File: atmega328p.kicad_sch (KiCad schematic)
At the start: 6 parts, among them J6 ICSP, U6 ATMEGA328PB-AU, Y1 CSTNE16M0VH3L000R0

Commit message: Replace CSTNE16M0VH3L000R0 ceramic resonator with HC49S quartz crystal and capacitors.
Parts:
- removed Y1: CSTNE16M0VH3L000R0, Crystal:Resonator_SMD_muRata_CSTxExxV-3Pin_3.0x1.1mm, symbol bkm-129x-scart-vga-rescue:Crystal_GND2
- added C14: 22pF, Capacitor_SMD:C_1206_3216Metric_Pad1.33x1.80mm_HandSolder, symbol bkm-129x-scart-vga-rescue:C
- added C18: 22pF, Capacitor_SMD:C_1206_3216Metric_Pad1.33x1.80mm_HandSolder, symbol Device:C
- added Y1: 16MHz, Crystal:Crystal_HC49-U_Vertical, symbol Device:Crystal
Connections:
- net GNDD: now also C14.2, C18.2
- net at U6.7 ((XTAL1/TOSC1)PB6): now also C14.1, Y1.2
- net at U6.8 ((XTAL2/TOSC2)PB7): now also C18.1, Y1.1

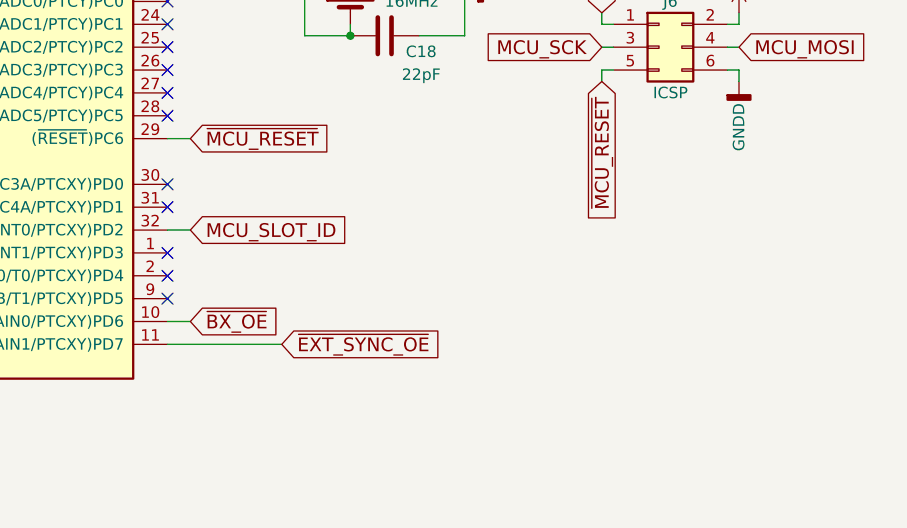
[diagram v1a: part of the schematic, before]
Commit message: Add debug UART connector to schematic and PCB. Edit silkscreen MCU description.
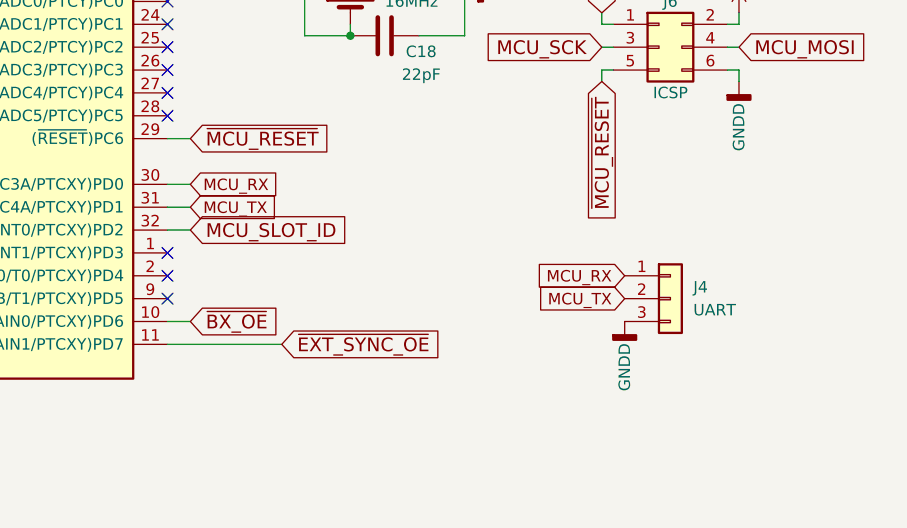
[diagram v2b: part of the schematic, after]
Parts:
- added J4: UART, Connector_PinHeader_2.54mm:PinHeader_1x03_P2.54mm_Vertical, symbol Connector_Generic:Conn_01x03
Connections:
- net GNDD: now also J4.3 (Pin_3)
- net MCU_RX: now reaches U6.30 ((RXD0/OC3A/PTCXY)PD0)
- net MCU_RX: now also J4.1 (Pin_1)
- net MCU_TX: now reaches U6.31 ((TXD0/OC4A/PTCXY)PD1)
- net MCU_TX: now also J4.2 (Pin_2)
- no-connect marks 17 -> 15
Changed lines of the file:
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@@
-	)
-	(no_connect
-		(at 163.83 101.6)
 	)
 	(no_connect
@@
 	)
 	(no_connect
-		(at 163.83 104.14)
-	)
-	(no_connect
 		(at 163.83 60.96)
 	)
@@
 	(wire
 		(pts
+			(xy 166.37 104.14) (xy 163.83 104.14)
+		)
+		(stroke
+			(width 0)
+			(type default)
+		)
+	)
+	(wire
+		(pts
 			(xy 163.83 96.52) (xy 166.37 96.52)
 		)
@@
 		(pts
 			(xy 184.15 74.93) (xy 184.15 76.2)
+		)
+		(stroke
+			(width 0)
+			(type default)
+		)
+	)
+	(wire
+		(pts
+			(xy 166.37 101.6) (xy 163.83 101.6)
 		)
 		(stroke
@@
 		)
 	)
+	(global_label "MCU_TX"
+		(shape input)
+		(at 214.63 114.3 180)
+		(fields_autoplaced yes)
+		(effects
+			(font
+				(size 1.27 1.27)
+			)
+			(justify right)
+		)
+		(property "Intersheetrefs" "${INTERSHEET_REFS}"
+			(at 205.1024 114.3 0)
+			(effects
+				(font
+					(size 1.27 1.27)
+				)
+				(justify right)
+				(hide yes)
+			)
+		)
+	)
 	(global_label "MCU_SCK"
 		(shape input)
@@
 		)
 	)
+	(global_label "MCU_RX"
+		(shape input)
+		(at 214.63 111.76 180)
+		(fields_autoplaced yes)
+		(effects
+			(font
+				(size 1.27 1.27)
+			)
+			(justify right)
+		)
+		(property "Intersheetrefs" "${INTERSHEET_REFS}"
+			(at 204.8 111.76 0)
+			(effects
+				(font
+					(size 1.27 1.27)
+				)
+				(justify right)
+				(hide yes)
+			)
+		)
+	)
 	(global_label "MCU_SLOT_ID"
 		(shape input)
@@
 		)
 	)
+	(global_label "MCU_RX"
+		(shape input)
+		(at 166.37 101.6 0)
+		(fields_autoplaced yes)
+		(effects
+			(font
+				(size 1.27 1.27)
+			)
+			(justify left)
+		)
+		(property "Intersheetrefs" "${INTERSHEET_REFS}"
+			(at 176.2 101.6 0)
+			(effects
+				(font
+					(size 1.27 1.27)
+				)
+				(justify left)
+				(hide yes)
+			)
+		)
+	)
 	(global_label "MCU_MISO"
 		(shape input)
@@
 					(size 1.27 1.27)
 				)
+				(hide yes)
+			)
+		)
+	)
+	(global_label "MCU_TX"
+		(shape input)
+		(at 166.37 104.14 0)
+		(fields_autoplaced yes)
+		(effects
+			(font
+				(size 1.27 1.27)
+			)
+			(justify left)
+		)
+		(property "Intersheetrefs" "${INTERSHEET_REFS}"
+			(at 175.8976 104.14 0)
+			(effects
+				(font
+					(size 1.27 1.27)
+				)
+				(justify left)
 				(hide yes)
 			)
@@
 				(path "/dd381a99-a14a-480e-874b-b22abf62e9bf/00000000-0000-0000-0000-00005fb20956"
 					(reference "C18")
+					(unit 1)
+				)
+			)
+		)
+	)
+	(symbol
+		(lib_id "bkm-129x-scart-vga-rescue:GNDD-power")
+		(at 214.63 116.84 0)
+		(unit 1)
+		(exclude_from_sim no)
+		(in_bom yes)
+		(on_board yes)
+		(dnp no)
+		(property "Reference" "#PWR06"
+			(at 214.63 123.19 0)
+			(effects
+				(font
+					(size 1.27 1.27)
+				)
+				(hide yes)
+			)
+		)
+		(property "Value" "GNDD"
+			(at 214.63 121.92 90)
+			(effects
+				(font
+					(size 1.27 1.27)
+				)
+			)
+		)
+		(property "Footprint" ""
+			(at 214.63 116.84 0)
+			(effects
+				(font
+					(size 1.27 1.27)
+				)
+				(hide yes)
+			)
+		)
+		(property "Datasheet" ""
+			(at 214.63 116.84 0)
+			(effects
+				(font
+					(size 1.27 1.27)
+				)
+				(hide yes)
+			)
+		)
+		(property "Description" ""
+			(at 214.63 116.84 0)
+			(effects
+				(font
+					(size 1.27 1.27)
+				)
+				(hide yes)
+			)
+		)
+		(pin "1"
+		)
+		(instances
+			(project "bkm-129x-scart-vga"
+				(path "/dd381a99-a14a-480e-874b-b22abf62e9bf/00000000-0000-0000-0000-00005fb20956"
+					(reference "#PWR06")
 					(unit 1)
 				)
@@
 					(unit 1)
 				)
+			)
+		)
+	)
+	(symbol
+		(lib_id "Connector_Generic:Conn_01x03")
+		(at 219.71 114.3 0)
+		(unit 1)
+		(exclude_from_sim no)
+		(in_bom yes)
+		(on_board yes)
+		(dnp no)
+		(fields_autoplaced yes)
+		(property "Reference" "J4"
+			(at 222.25 113.0299 0)
+			(effects
+				(font
+					(size 1.27 1.27)
+				)
+				(justify left)
+			)
+		)
+		(property "Value" "UART"
+			(at 222.25 115.5699 0)
+			(effects
+				(font
+					(size 1.27 1.27)
+				)
+				(justify left)
+			)
+		)
+		(property "Footprint" "Connector_PinHeader_2.54mm:PinHeader_1x03_P2.54mm_Vertical"
+			(at 219.71 114.3 0)
+			(effects
+				(font
+					(size 1.27 1.27)
+				)
+				(hide yes)
+			)
+		)
+		(property "Datasheet" "~"
+			(at 219.71 114.3 0)
+			(effects
+				(font
+					(size 1.27 1.27)
+				)
+				(hide yes)
+			)
+		)
+		(property "Description" "Generic connector, single row, 01x03, script generated (kicad-library-utils/schlib/autogen/connector/)"
+			(at 219.71 114.3 0)
+			(effects
+				(font
+					(size 1.27 1.27)
+				)
+				(hide yes)
+			)
+		)
+		(pin "3"
+		)
+		(pin "2"
+		)
+		(pin "1"
+		)
+		(instances
+			(project "bkm-129x-scart-vga"
+				(path "/dd381a99-a14a-480e-874b-b22abf62e9bf/00000000-0000-0000-0000-00005fb20956"
+					(reference "J4")
+					(unit 1)
+				)

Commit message: Change C14, C18 footprints from 1206 to 0805.
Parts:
- C14, C18: footprint Capacitor_SMD:C_1206_3216Metric_Pad1.33x1.80mm_HandSolder -> Capacitor_SMD:C_0805_2012Metric_Pad1.18x1.45mm_HandSolder
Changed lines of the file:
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@@
 			)
 		)
-		(property "Footprint" "Capacitor_SMD:C_1206_3216Metric_Pad1.33x1.80mm_HandSolder"
+		(property "Footprint" "Capacitor_SMD:C_0805_2012Metric_Pad1.18x1.45mm_HandSolder"
 			(at 191.77 84.1248 0)
 			(effects
@@
 			)
 		)
-		(property "Footprint" "Capacitor_SMD:C_1206_3216Metric_Pad1.33x1.80mm_HandSolder"
+		(property "Footprint" "Capacitor_SMD:C_0805_2012Metric_Pad1.18x1.45mm_HandSolder"
 			(at 191.77 73.9648 0)
 			(effects
